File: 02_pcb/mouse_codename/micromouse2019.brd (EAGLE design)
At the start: 45 x 50 mm, 71 parts

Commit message: merge fixed
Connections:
- net GND: no longer IRD:MOSFET1.P1, IRD:MOSFET1.P4, IRD:MOSFET2.P1, IRD:MOSFET2.P4, IRD:R1.1, IRD:R2.1, IRD:R3.1, IRD:R4.1, IRD:R5.1, IRD:R6.1, IRD:R7.1, IRD:R8.1

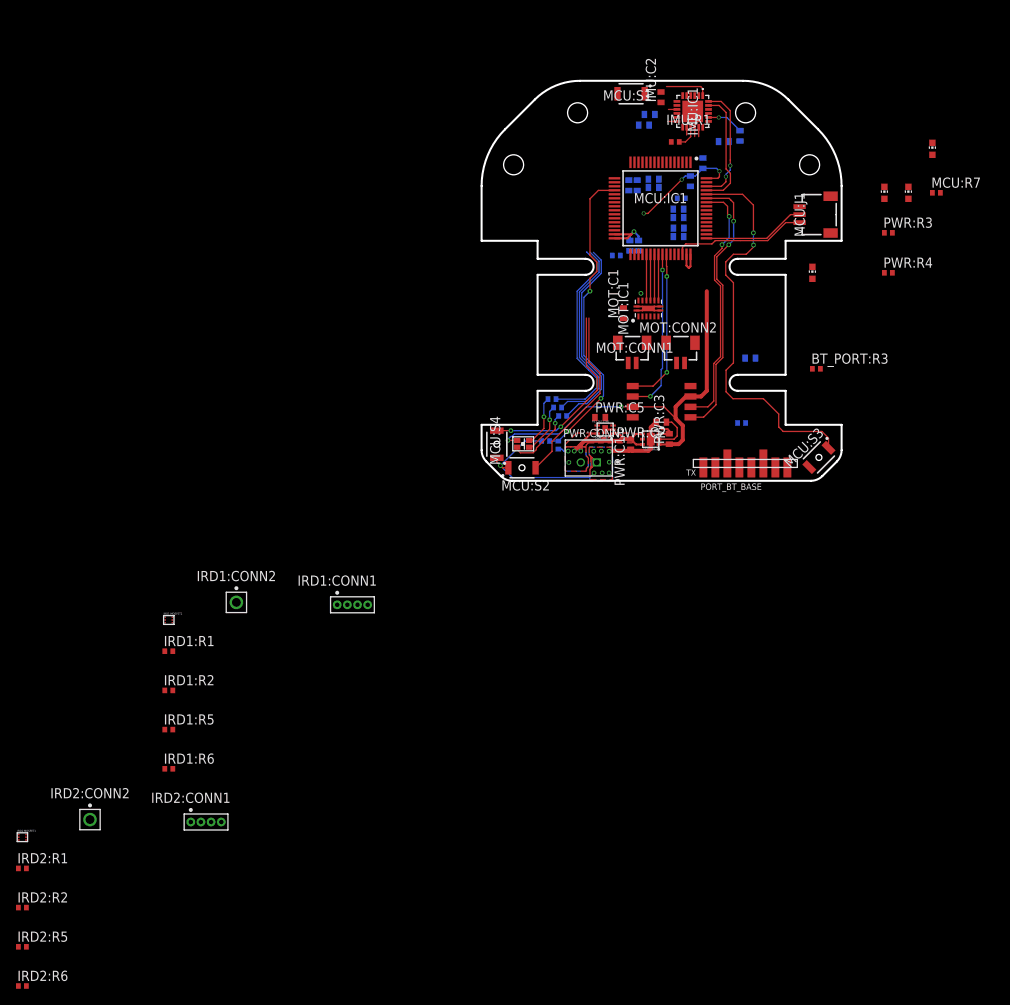
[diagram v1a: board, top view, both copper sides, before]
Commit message: replaced pins
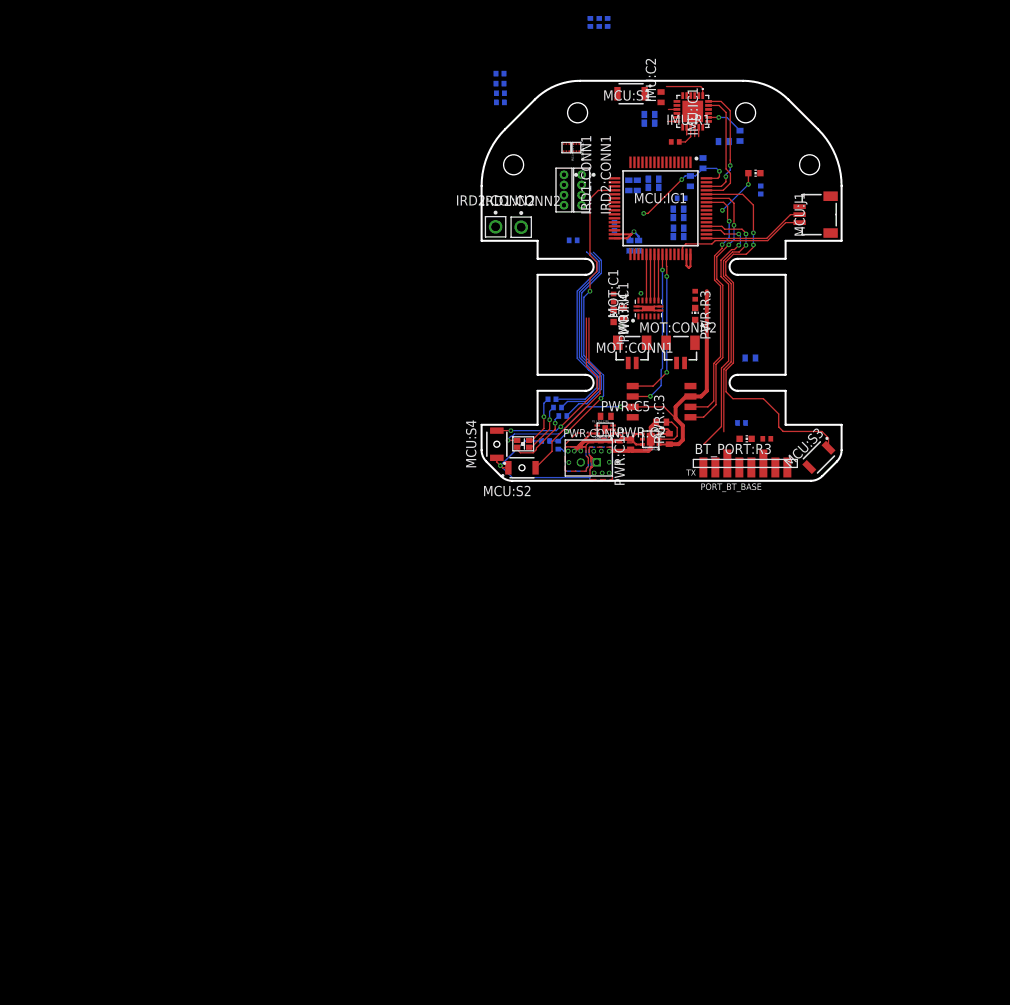
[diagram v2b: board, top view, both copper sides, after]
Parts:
- BT_PORT:R3: device rcl:R0402 -> 0-micromouse2019:R0402
- MCU:S2: value BTN_B3U-3000P -> BTN1
- MCU:S3: value BTN_B3U-3000P -> BTN_B3U-1000P; device 0-micromouse2019:B3U-3000P -> 0-micromouse2019:B3U-1000P
- MCU:S4: value BTN_B3U-3000P -> BTN2
- moved IRD2:R6 125.6 mm to (2.35, 47.3), flipped to the bottom
- moved IRD2:R5 122.3 mm to (2.35, 48.5), flipped to the bottom
- moved IRD2:R2 119.1 mm to (2.30, 49.6), flipped to the bottom
- moved IRD2:R1 115.9 mm to (2.30, 50.9), flipped to the bottom
- moved IRD2:MOSFET1 110.6 mm to (11.8, 41.6), turned to 270 degrees
- moved IRD1:R6 107.7 mm to (14.7, 57.3), flipped to the bottom, turned to 90 degrees
- moved IRD1:R5 104.0 mm to (15.8, 57.3), flipped to the bottom, turned to 90 degrees
- moved IRD1:R1 94.6 mm to (13.6, 57.3), flipped to the bottom, turned to 90 degrees
- moved IRD2:CONN1 94.5 mm to (12.5, 38.2), turned to 270 degrees
- moved IRD2:CONN2 89.8 mm to (1.75, 31.8)
- moved IRD1:MOSFET1 77.2 mm to (10.6, 41.6), turned to 270 degrees
- moved IRD1:R2 75.6 mm to (11.4, 30.1), flipped to the bottom, turned to 180 degrees
- moved IRD1:CONN1 60.8 mm to (10.3, 38.2), turned to 270 degrees
- moved IRD1:CONN2 58.9 mm to (4.95, 31.7)
- moved PWR:LED2 37.2 mm to (16.5, 20.6)
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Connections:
- new net MCU:N$5: MCU:IC1.56
- new net MCU:N$6: MCU:IC1.57
- net MCU:BTN1: now also MCU:IC1.34; no longer MCU:IC1.55
- net MCU:BTN2: now also MCU:IC1.33; no longer MCU:IC1.56
- net MCU:HEARTBEAT: now also MCU:IC1.55; no longer MCU:IC1.33
- net MCU:RGB_B: now also MCU:IC1.27; no longer MCU:IC1.23
- net MCU:RGB_G: now also MCU:IC1.26; no longer MCU:IC1.27
- net MCU:RGB_R: now also MCU:IC1.23; no longer MCU:IC1.26
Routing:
- net UART3_TX: track 0.00 -> 33.5 mm, vias 0 -> 2
- net UART3_RX: track 0.00 -> 32.5 mm, vias 0 -> 2
- net MCU:HEARTBEAT: track 0.00 -> 6.01 mm, vias 0 -> 2

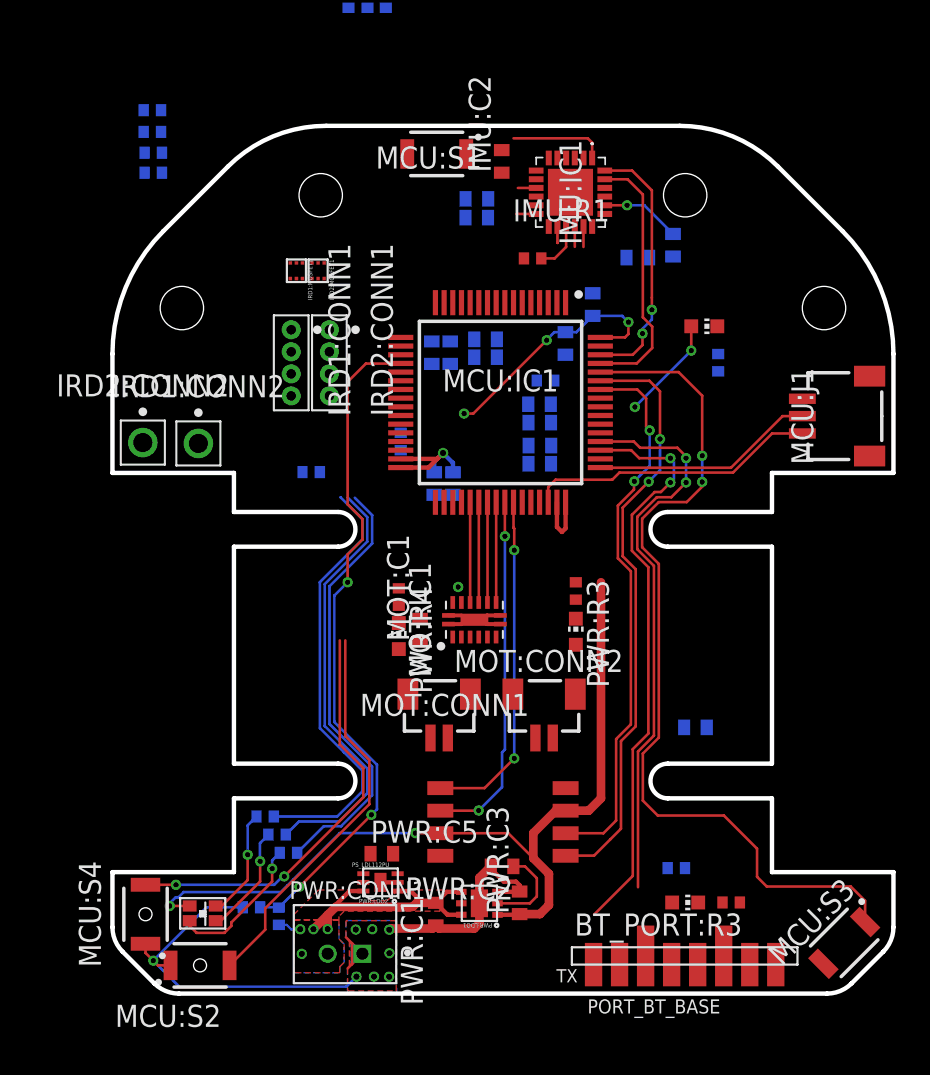
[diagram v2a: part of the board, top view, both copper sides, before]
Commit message: vcc routed
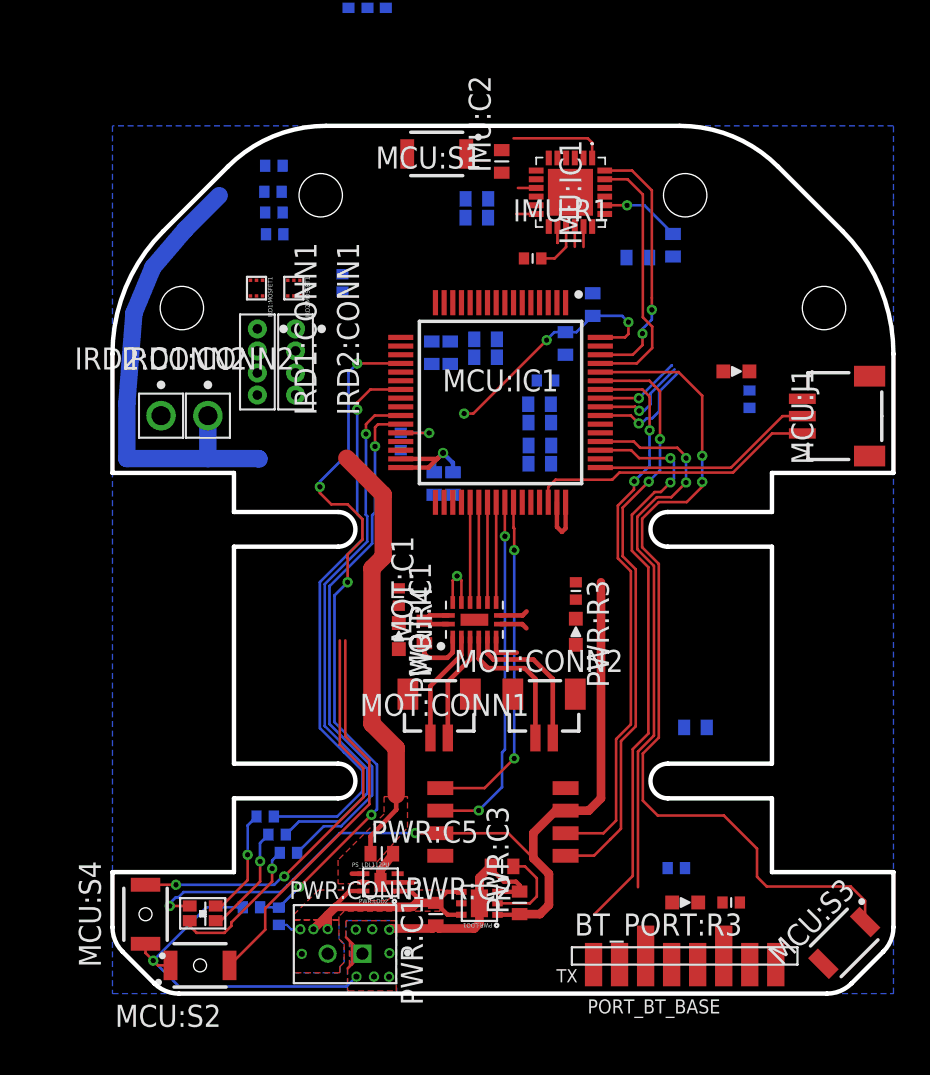
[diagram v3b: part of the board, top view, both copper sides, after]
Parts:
- moved IRD1:R2 11.0 mm to (13.2, 41.0), turned to 270 degrees
- moved IRD2:R1 8.39 mm to (9.25, 46.2)
- moved IRD2:R6 7.85 mm to (9.35, 43.8)
- moved IRD2:R5 7.76 mm to (9.30, 45.0)
- moved IRD2:R2 7.27 mm to (9.30, 47.7)
- moved MCU:LED1 3.19 mm to (36.0, 35.9)
- moved MCU:R7 2.77 mm to (36.7, 34.2)
- moved IRD1:MOSFET1 2.51 mm to (8.30, 40.6)
- moved IRD1:CONN1 1.95 mm to (8.35, 38.3)
- moved IRD2:CONN1 1.95 mm to (10.6, 38.3)
- moved IRD2:CONN2 1.87 mm to (2.80, 33.3)
- moved IRD2:MOSFET1 1.72 mm to (10.4, 40.6)
- moved IRD1:CONN2 1.69 mm to (5.50, 33.3)
- moved MOT:C1 0.27 mm to (18.0, 20.8)
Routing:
- net VCC: track 0.00 -> 56.1 mm
- net MOT:BOUT2: track 0.00 -> 8.72 mm
- net MOT:BOUT1: track 0.00 -> 8.40 mm
- net MCU:RGB_R: track 25.2 -> 33.1 mm, vias 0 -> 1
- net MOT:AOUT1: track 0.00 -> 6.55 mm
- net MOT:AOUT2: track 0.00 -> 6.35 mm
- net MCU:RGB_G: track 25.2 -> 31.2 mm, vias 0 -> 1
- net GND: track 51.8 -> 57.7 mm
- net MCU:N$5: track 0.00 -> 5.73 mm, vias 0 -> 1
- net MCU:RGB_B: track 25.3 -> 30.6 mm, vias 0 -> 1
- net MCU:N$6: track 0.00 -> 4.91 mm, vias 0 -> 1
- net MCU:BOOT1: track 0.00 -> 3.29 mm, vias 0 -> 1
- net +3V3: track 77.0 -> 80.2 mm
- net V_BAT_LEVEL: track 39.3 -> 41.4 mm, vias 3 -> 5
- net MCU:HEARTBEAT: track 6.01 -> 6.60 mm, vias 2 -> 1
- added copper zone on layer 1, net VCC

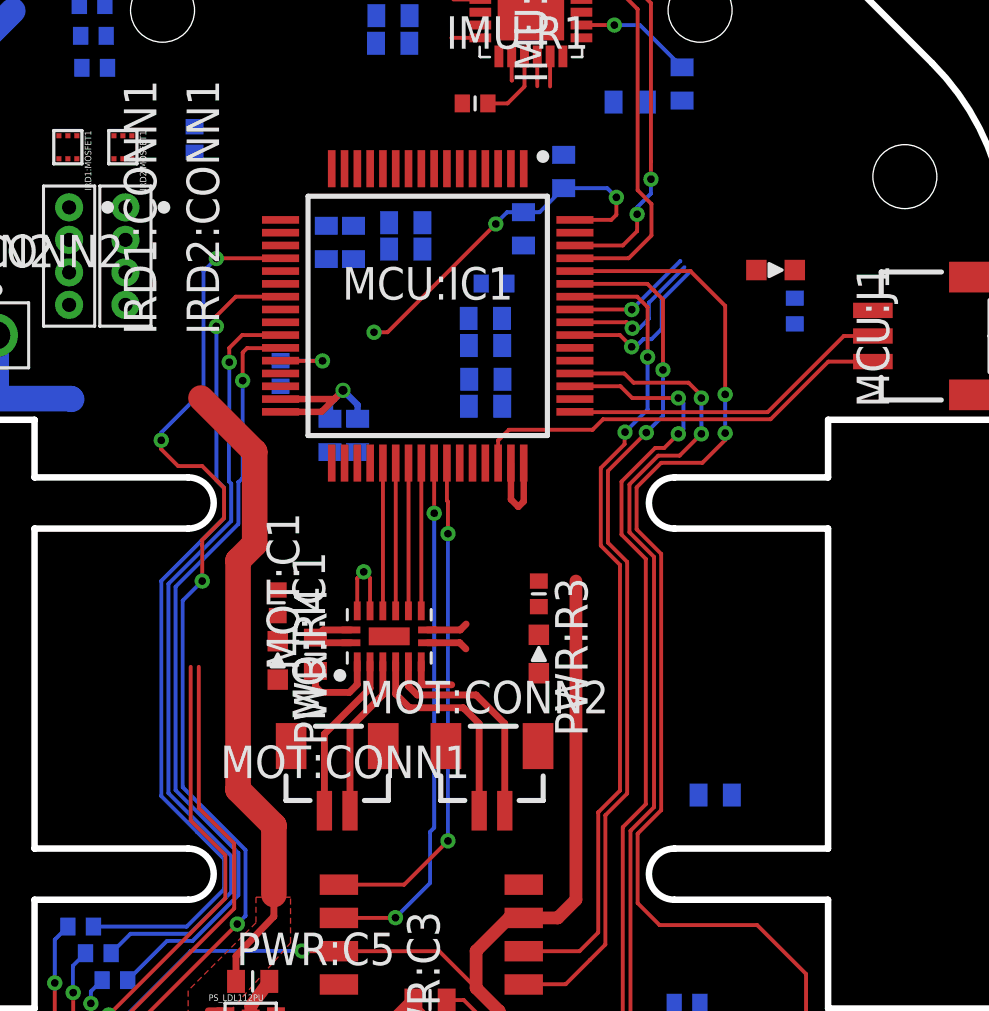
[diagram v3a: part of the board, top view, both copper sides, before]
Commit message: leds added
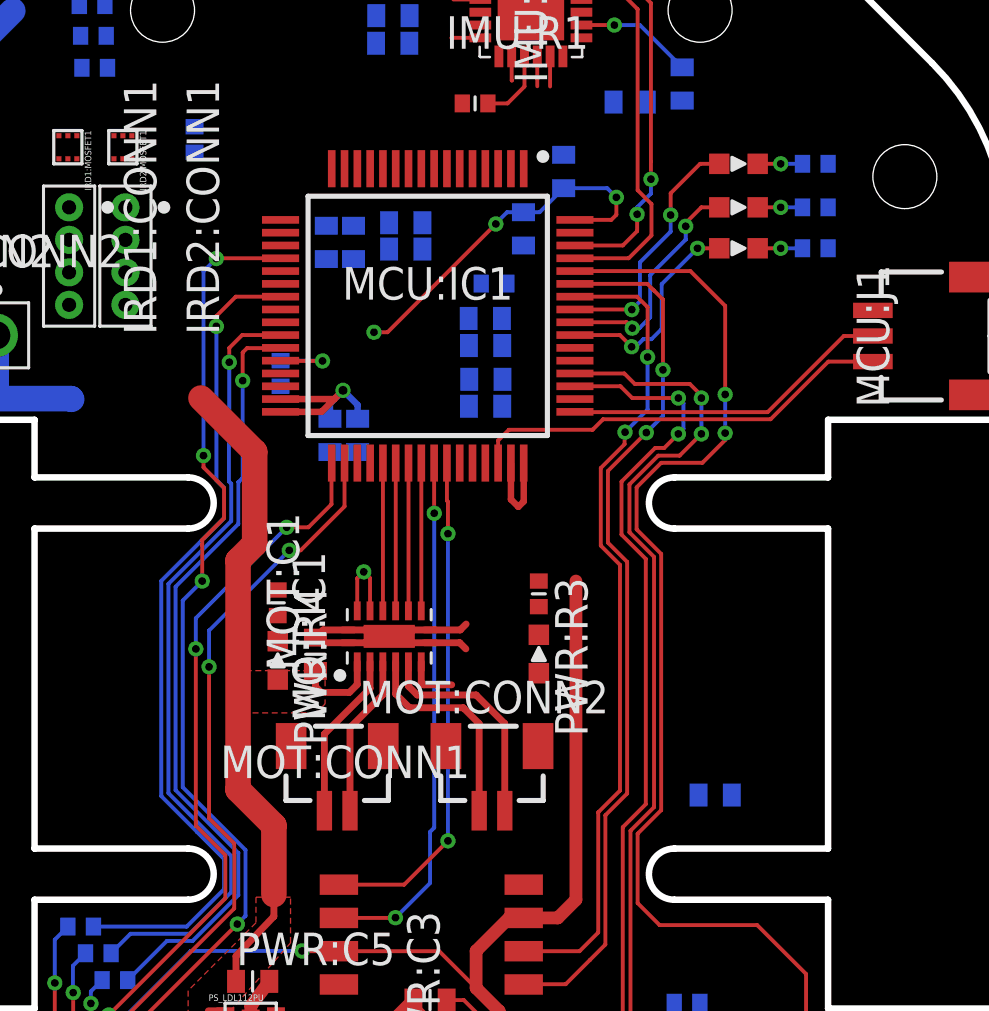
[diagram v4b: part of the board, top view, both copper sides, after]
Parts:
- added MCU:LED2: LED_GREEN, 0-micromouse2019:CHIP-LED0603
- added MCU:LED3: LED_YELLOW, 0-micromouse2019:CHIP-LED0603
- added MCU:R8: 100R, 0-micromouse2019:R0402
- added MCU:R9: 270R, 0-micromouse2019:R0402
- MCU:LED1: value LED_GREEN -> LED_PINK
- moved MCU:R7 4.13 mm to (37.5, 38.3), turned to 180 degrees
- moved MCU:LED1 2.85 mm to (34.5, 38.3)
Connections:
- new net MCU:LED_PINK: MCU:IC1.56, MCU:LED1.A
- new net MCU:LED_YELLOW_SUBMARINE: MCU:IC1.57, MCU:LED3.A
- net GND: now also MCU:R8.2, MCU:R9.2
- net MCU:HEARTBEAT: now also MCU:LED2.A; no longer MCU:LED1.A
- net MCU:N$5: now also MCU:LED2.C, MCU:R8.1; no longer MCU:IC1.56
- net MCU:N$6: now also MCU:LED3.C, MCU:R9.1; no longer MCU:IC1.57
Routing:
- net MCU:BTN2: track 24.2 -> 34.8 mm, vias 2 -> 4
- net MCU:BTN1: track 22.6 -> 32.9 mm, vias 0 -> 2
- net MCU:LED_YELLOW_SUBMARINE: track 0.00 -> 9.77 mm, vias 0 -> 2
- net MCU:LED_PINK: track 0.00 -> 9.05 mm, vias 0 -> 2
- net MCU:N$5: track 5.73 -> 1.75 mm
- net MCU:N$6: track 4.91 -> 1.75 mm
- net V_BAT_LEVEL: track 41.4 -> 39.5 mm
- net MCU:HEARTBEAT: track 6.60 -> 8.45 mm, vias 1 -> 2
- net MCU:N$2: track 0.00 -> 1.75 mm, vias 0 -> 1
- net GND: track 57.7 -> 58.2 mm
